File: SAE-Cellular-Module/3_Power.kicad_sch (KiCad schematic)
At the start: 45 parts, among them Q6 PMOS, U2 TPS26600RHF, U3 LDL1117S33R, U4 TPS54202DDC

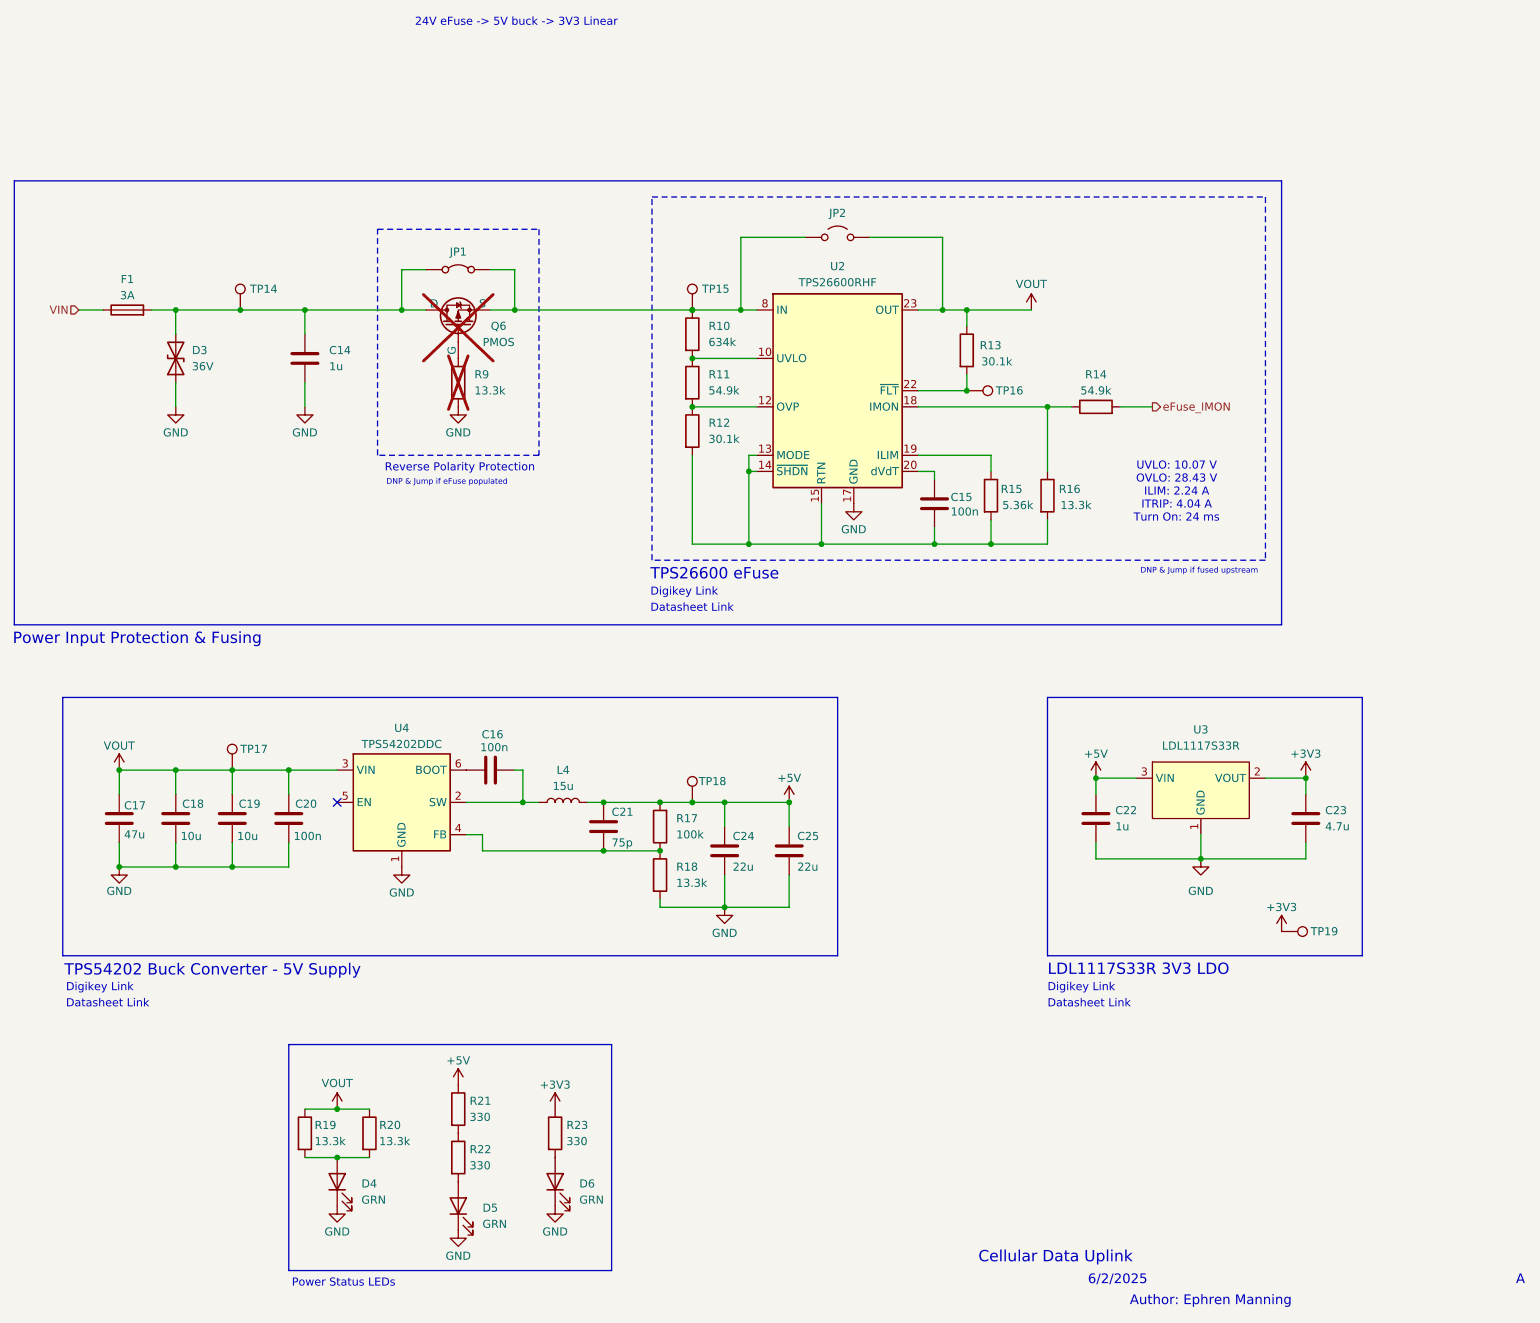
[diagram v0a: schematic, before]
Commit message: Added initial component placements
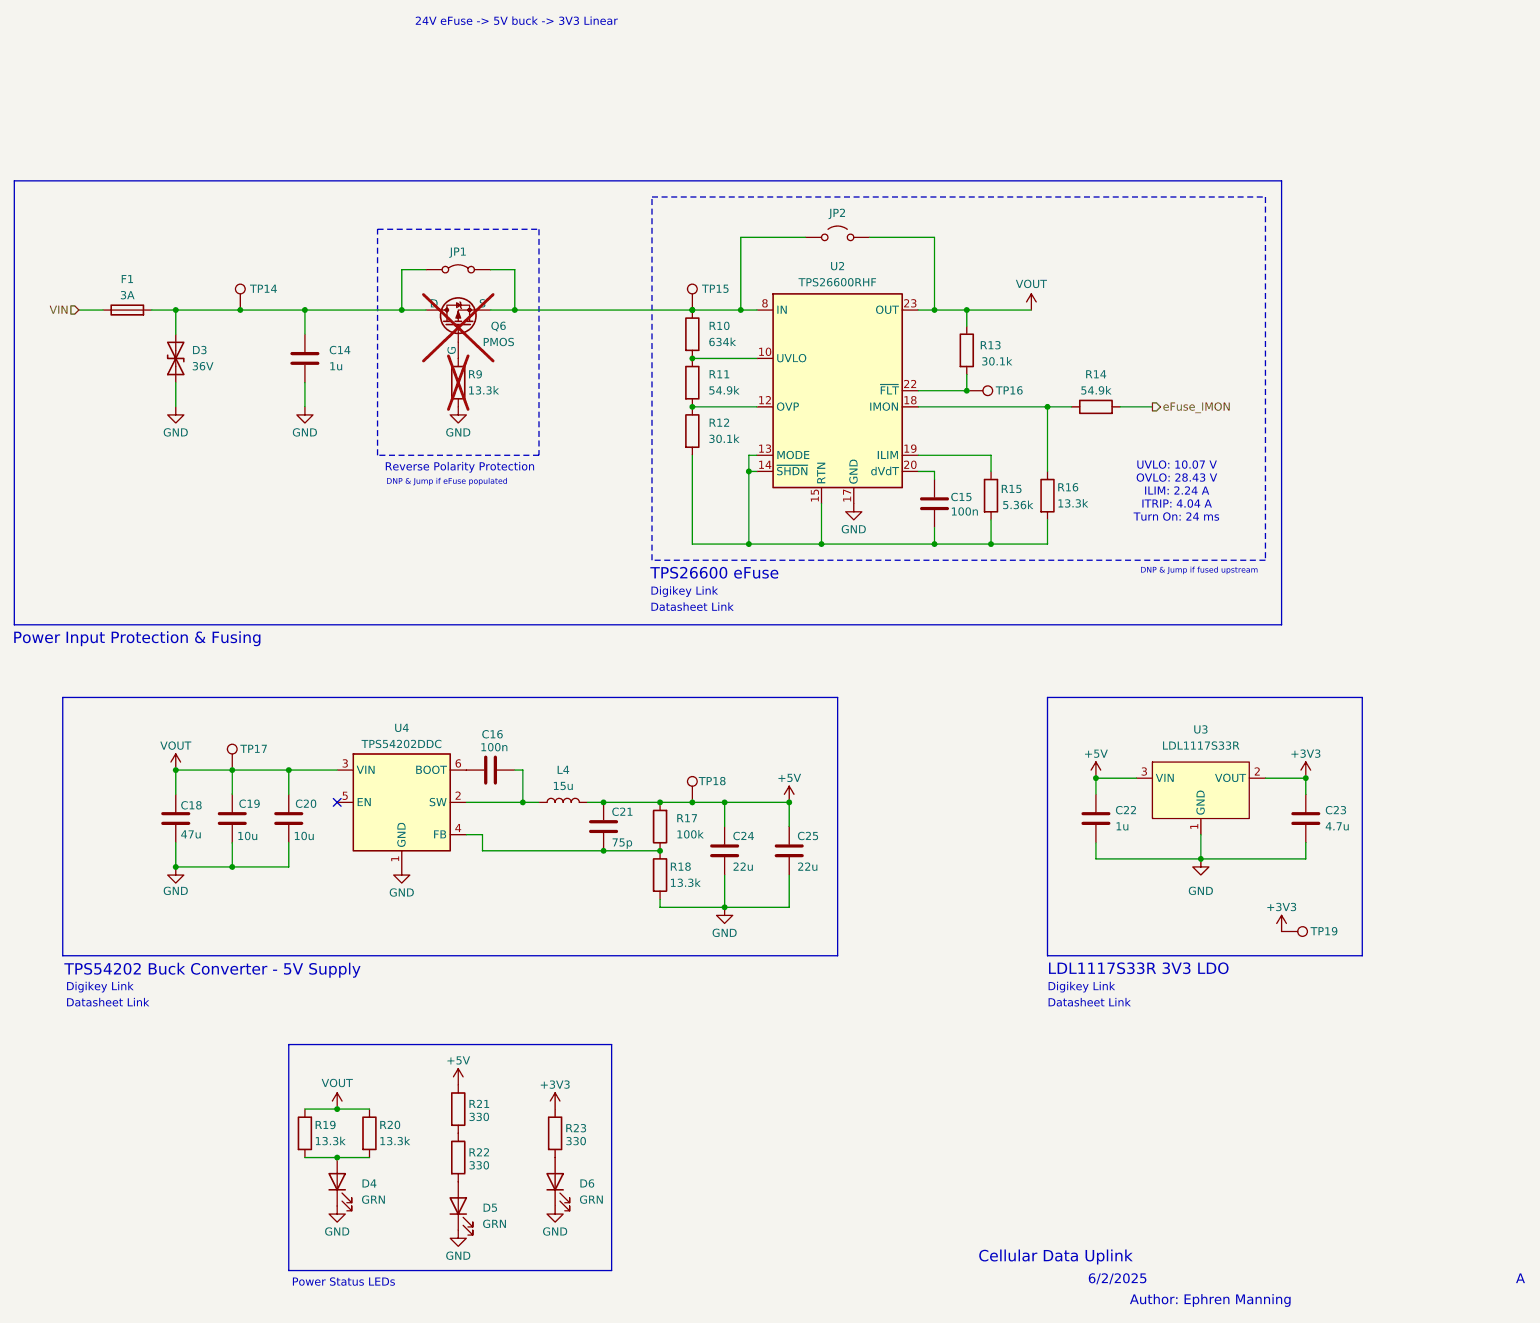
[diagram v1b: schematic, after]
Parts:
- removed C17: 47u, Capacitor_SMD:C_Elec_6.3x5.4, symbol Device:C
- removed C19: 10u, Capacitor_SMD:C_1210_3225Metric, symbol Device:C
- added C18: 47u, Capacitor_SMD:C_Elec_6.3x5.4, symbol Device:C
- C19: renamed from C18; footprint Capacitor_SMD:C_1210_3225Metric -> Capacitor_SMD:C_0805_2012Metric; MPN CL32B106KBJNNNE -> GRM21BR6YA106KE43L
- C20: value 100n -> 10u; footprint Capacitor_SMD:C_0603_1608Metric -> Capacitor_SMD:C_0805_2012Metric; MPN GCM188R71H104KA57J -> GRM21BR6YA106KE43L
- C23: footprint Capacitor_SMD:C_0805_2012Metric -> Capacitor_SMD:C_0603_1608Metric; MPN CL21A475KPFNNNE -> CL10A475KP8NNNC
- R10: footprint (none) -> Resistor_SMD:R_0402_1005Metric; MPN (none) -> RC0402FR-07634KL
- R11, R14: footprint (none) -> Resistor_SMD:R_0402_1005Metric; MPN (none) -> RC0402FR-1354K9L
- R12, R13: footprint (none) -> Resistor_SMD:R_0402_1005Metric; MPN (none) -> RC0402FR-0730K1L
- R15: footprint (none) -> Resistor_SMD:R_0402_1005Metric; MPN (none) -> RMCF0402FT5K36
- R16, R18, R19, R20, R9: footprint (none) -> Resistor_SMD:R_0402_1005Metric; MPN (none) -> ERJ-2RKF1332X
- R17: footprint (none) -> Resistor_SMD:R_0402_1005Metric; MPN (none) -> ERJ-2RKF1003X
- R21, R22, R23: footprint (none) -> Resistor_SMD:R_0402_1005Metric; MPN (none) -> ERJ-2RKF3300X
- TP14, TP15, TP16, TP17, TP18, TP19: footprint (none) -> TestPoint:TestPoint_Pad_D1.0mm
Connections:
- net GND: now also C18.2
- net VOUT: now also C18.1
- net at JP1.2 (B), JP2.1 (A), Q6.3 (S)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: now also Q6.1 (S), Q6.2 (S)
- net at C14.1, D3.2 (A2), F1.2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: now also Q6.5 (D), Q6.6 (D), Q6.7 (D), Q6.8 (D); no longer Q6.1 (D)
- net at R9.1: now also Q6.4 (G); no longer Q6.2 (G)
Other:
- moved on the sheet: C19
